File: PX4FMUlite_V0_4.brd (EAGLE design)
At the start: 48.6 x 34.9 mm, 126 parts, among them J2 DF13-4P-1.25V, J201 DF13C-6P-1.25V, J202 DF13C-6P-1.25V, J203 DF13C-6P-1.25V, J3 DF13C-4P-1.25V, J302 DF13C-4P-1.25V, J401 DF13C-4P-1.25V, J403 DF13C-7P-1.25V, J405 DF13C-4P-1.25V, J802 DF13C-3P-1.25V, M3_MOUNT1101 MOUNT-HOLE3.1MM, M3_MOUNT1102 MOUNT-HOLE3.1MM, M3_MOUNT1103 MOUNT-HOLE3.1MM, M3_MOUNT1104 MOUNT-HOLE3.1MM, U101 STM32F4X7VX, U2 MAX3051, U401 MAX3051, X101 3.2x2.5 mm / 24 MHz / 15 ppm

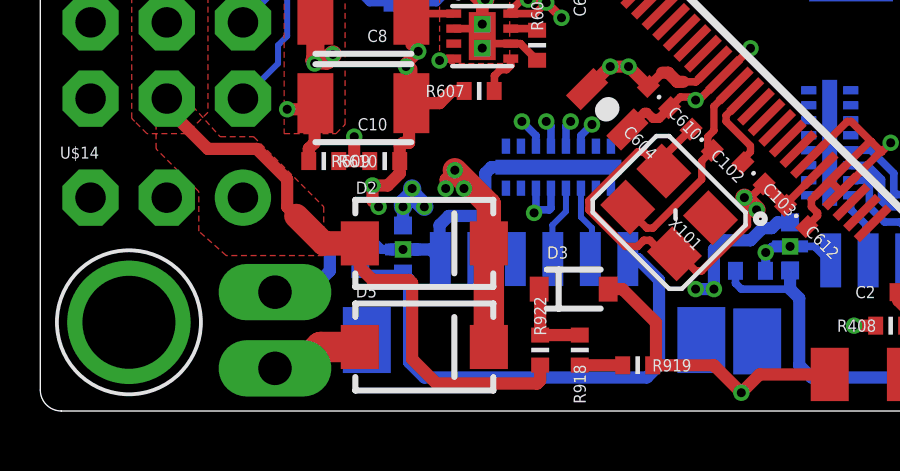
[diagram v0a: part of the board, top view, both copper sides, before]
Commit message: Voltage sense moved from VSERVO to VAUX
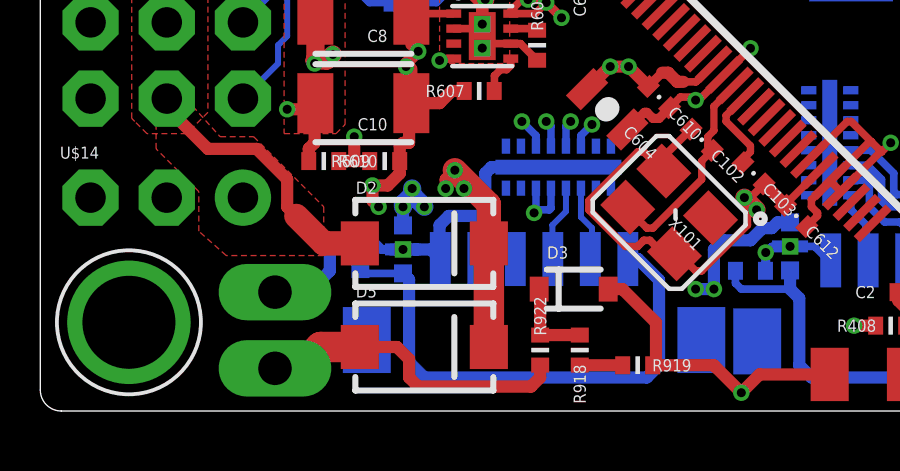
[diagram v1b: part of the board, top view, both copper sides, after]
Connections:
- net V_EXT: now also R922.P$2
- net V_SERVO: no longer R922.P$2
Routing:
- net V_SERVO: track 19.6 -> 9.15 mm
- net V_EXT: track 3.12 -> 10.6 mm
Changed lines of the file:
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@@
 <layer number="17" name="Pads" color="2" fill="1" visible="yes" active="yes"/>
 <layer number="18" name="Vias" color="2" fill="1" visible="yes" active="yes"/>
-<layer number="19" name="Unrouted" color="14" fill="1" visible="no" active="yes"/>
+<layer number="19" name="Unrouted" color="14" fill="1" visible="yes" active="yes"/>
 <layer number="20" name="Dimension" color="15" fill="1" visible="yes" active="yes"/>
 <layer number="21" name="tPlace" color="7" fill="1" visible="yes" active="yes"/>
@@
 <wire x1="18.5928" y1="4.8768" x2="17.8816" y2="4.1656" width="1.016" layer="1"/>
 <wire x1="17.8816" y1="4.1656" x2="17.0688" y2="4.1656" width="1.016" layer="1"/>
+<contactref element="R922" pad="P$2"/>
+<wire x1="25.908" y1="4.2752" x2="25.908" y2="3.8608" width="0.4064" layer="1"/>
+<wire x1="25.908" y1="3.8608" x2="25.6032" y2="3.556" width="0.4064" layer="1"/>
+<wire x1="25.6032" y1="3.556" x2="21.844" y2="3.556" width="0.4064" layer="1"/>
+<wire x1="21.844" y1="3.556" x2="21.5392" y2="3.8608" width="0.4064" layer="1"/>
+<wire x1="21.5392" y1="3.8608" x2="21.5392" y2="4.4704" width="0.4064" layer="1"/>
+<wire x1="21.5392" y1="4.4704" x2="21.1328" y2="4.8768" width="0.4064" layer="1"/>
+<wire x1="21.1328" y1="4.8768" x2="19.8972" y2="4.8768" width="0.4064" layer="1"/>
 </signal>
 <signal name="N$10">
@@
 </signal>
 <signal name="V_SERVO" class="1">
-<contactref element="R922" pad="P$2"/>
 <contactref element="D2" pad="A"/>
 <contactref element="J1" pad="PWR_S4"/>
@@
 <vertex x="12.2936" y="12.4968"/>
 </polygon>
-<wire x1="25.908" y1="4.2752" x2="25.908" y2="3.7592" width="0.4064" layer="1"/>
-<wire x1="25.908" y1="3.7592" x2="25.8064" y2="3.6576" width="0.4064" layer="1"/>
-<wire x1="25.8064" y1="3.6576" x2="22.4536" y2="3.6576" width="0.4064" layer="1"/>
-<wire x1="22.4536" y1="3.6576" x2="21.6408" y2="4.4704" width="0.4064" layer="1"/>
-<wire x1="21.6408" y1="4.4704" x2="21.6408" y2="7.0104" width="0.4064" layer="1"/>
-<wire x1="21.6408" y1="7.0104" x2="21.5392" y2="7.112" width="0.4064" layer="1"/>
-<wire x1="21.5392" y1="7.112" x2="20.32" y2="7.112" width="0.4064" layer="1"/>
-<wire x1="20.32" y1="7.112" x2="19.8972" y2="7.5348" width="0.4064" layer="1"/>
-<wire x1="19.8972" y1="7.5348" x2="19.8972" y2="8.3312" width="0.4064" layer="1"/>
 </signal>
 <signal name="FMU-CH9">
